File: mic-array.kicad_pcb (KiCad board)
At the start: 2 copper layers, 150 x 150 mm, 70 parts, among them J1 CON40A, K1 74LV244, U1 MIC, U10 MIC, U11 MIC, U12 MIC, U13 MIC, U14 MIC, U15 MIC, U16 MIC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

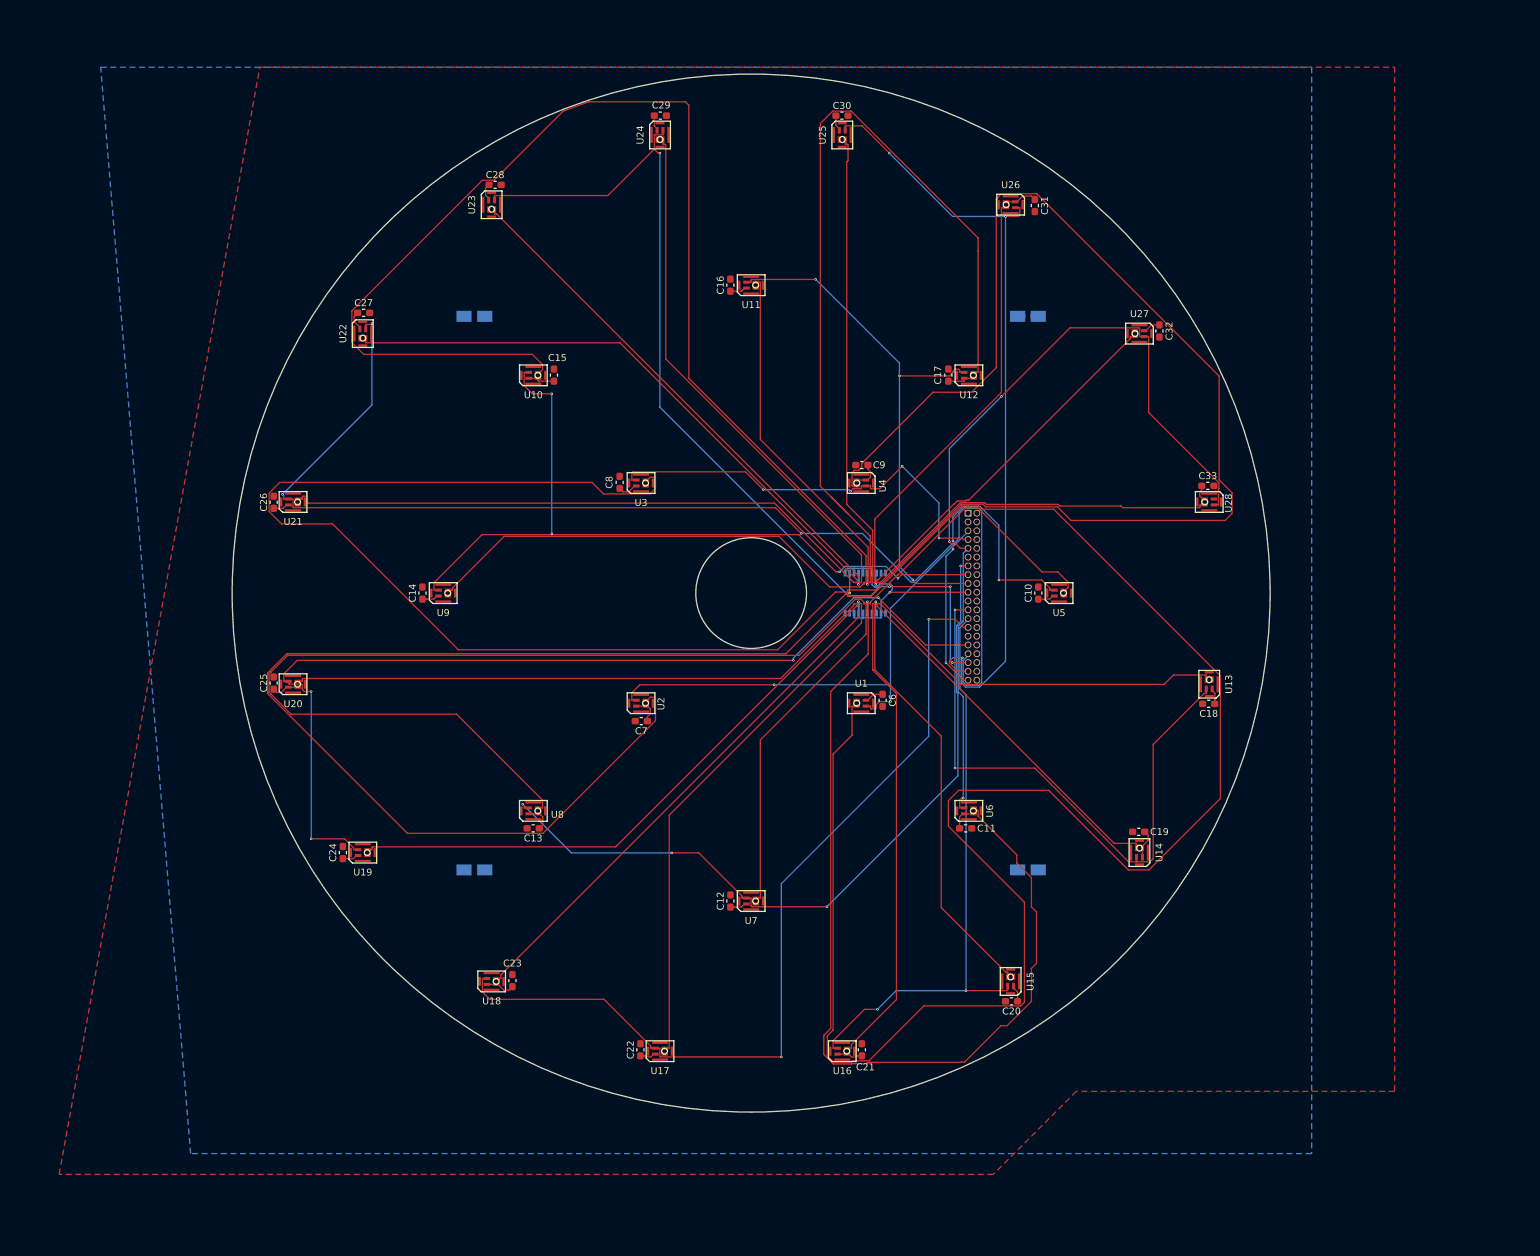
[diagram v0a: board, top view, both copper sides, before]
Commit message: Add new PCB design with improved constraints and routing. Change connector type to 2.54mm one.
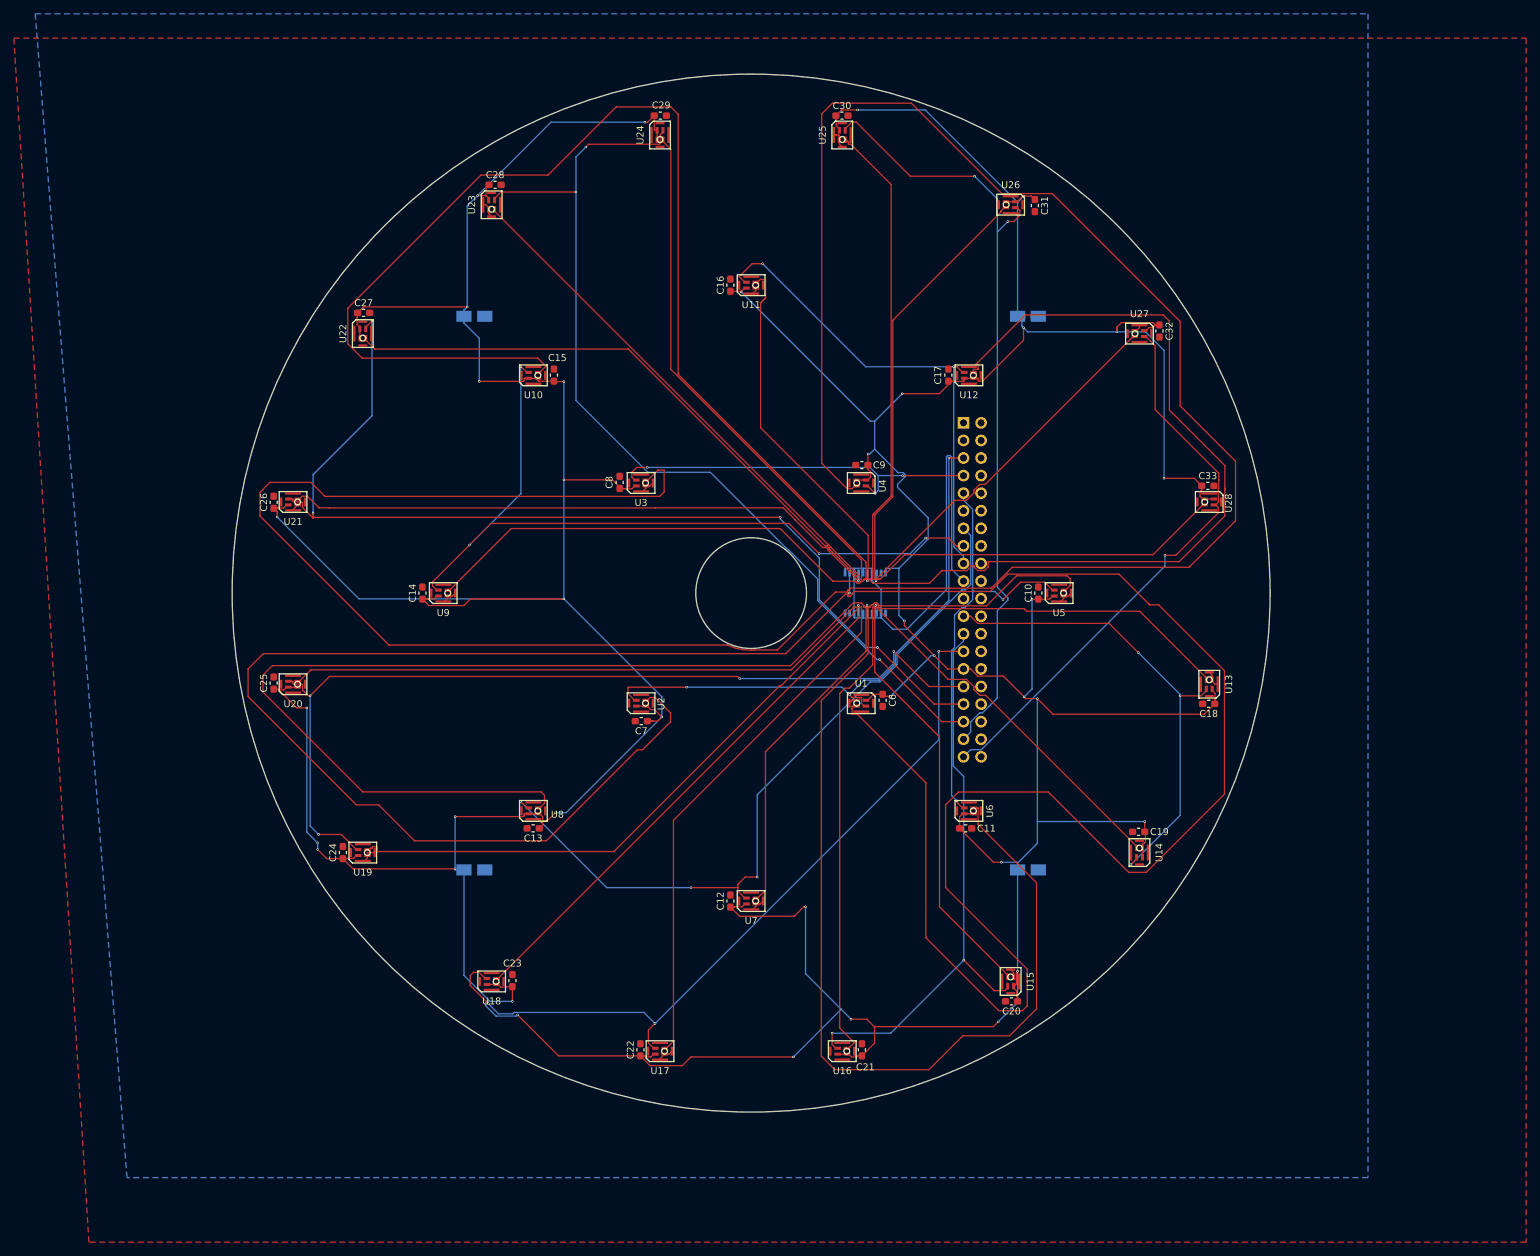
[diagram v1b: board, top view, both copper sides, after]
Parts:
- J1: footprint Connector_PinSocket_1.27mm:PinSocket_2x20_P1.27mm_Vertical -> Connector_PinSocket_2.54mm:PinSocket_2x20_P2.54mm_Vertical
- moved J1 13.1 mm to (180.7, 75.4)
- moved RN2 0.50 mm to (165.5, 102.0)
- moved RN3 0.50 mm to (166.8, 102.0)
- moved RN4 0.50 mm to (165.5, 98.0)
- moved RN5 0.50 mm to (166.8, 98.0)
- moved RN6 0.50 mm to (168.0, 98.0)
- moved RN7 0.50 mm to (168.0, 102.0)
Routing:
- net +3V3: track 87.9 -> 900.7 mm, vias 0 -> 38
- net /CLKIN: track 34.0 -> 77.8 mm, vias 1 -> 0
- net /CLK0_3: track 180.5 -> 215.1 mm
- net /CLK0_0: track 254.9 -> 222.7 mm
- net /DATA10: track 177.8 -> 148.2 mm, vias 3 -> 4
- net GND: track 0.00 -> 28.7 mm
- net /DATA13: track 102.3 -> 83.1 mm, vias 4 -> 1
- net /DATA6: track 87.8 -> 69.3 mm, vias 2 -> 3
- net /DATA8: track 128.8 -> 112.4 mm, vias 2 -> 3
- net /CLK0_1: track 167.8 -> 177.8 mm
- net /DATA9: track 141.7 -> 132.2 mm
- net /DATA0: track 73.6 -> 82.0 mm, vias 2 -> 3
- net /DATA2: track 70.6 -> 62.5 mm, vias 3 -> 2
- net /DATA5: track 78.0 -> 70.2 mm, vias 3 -> 2
- net /CLK0_2: track 158.6 -> 166.1 mm
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
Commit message: Add a new buffer to compensate nets impedance.
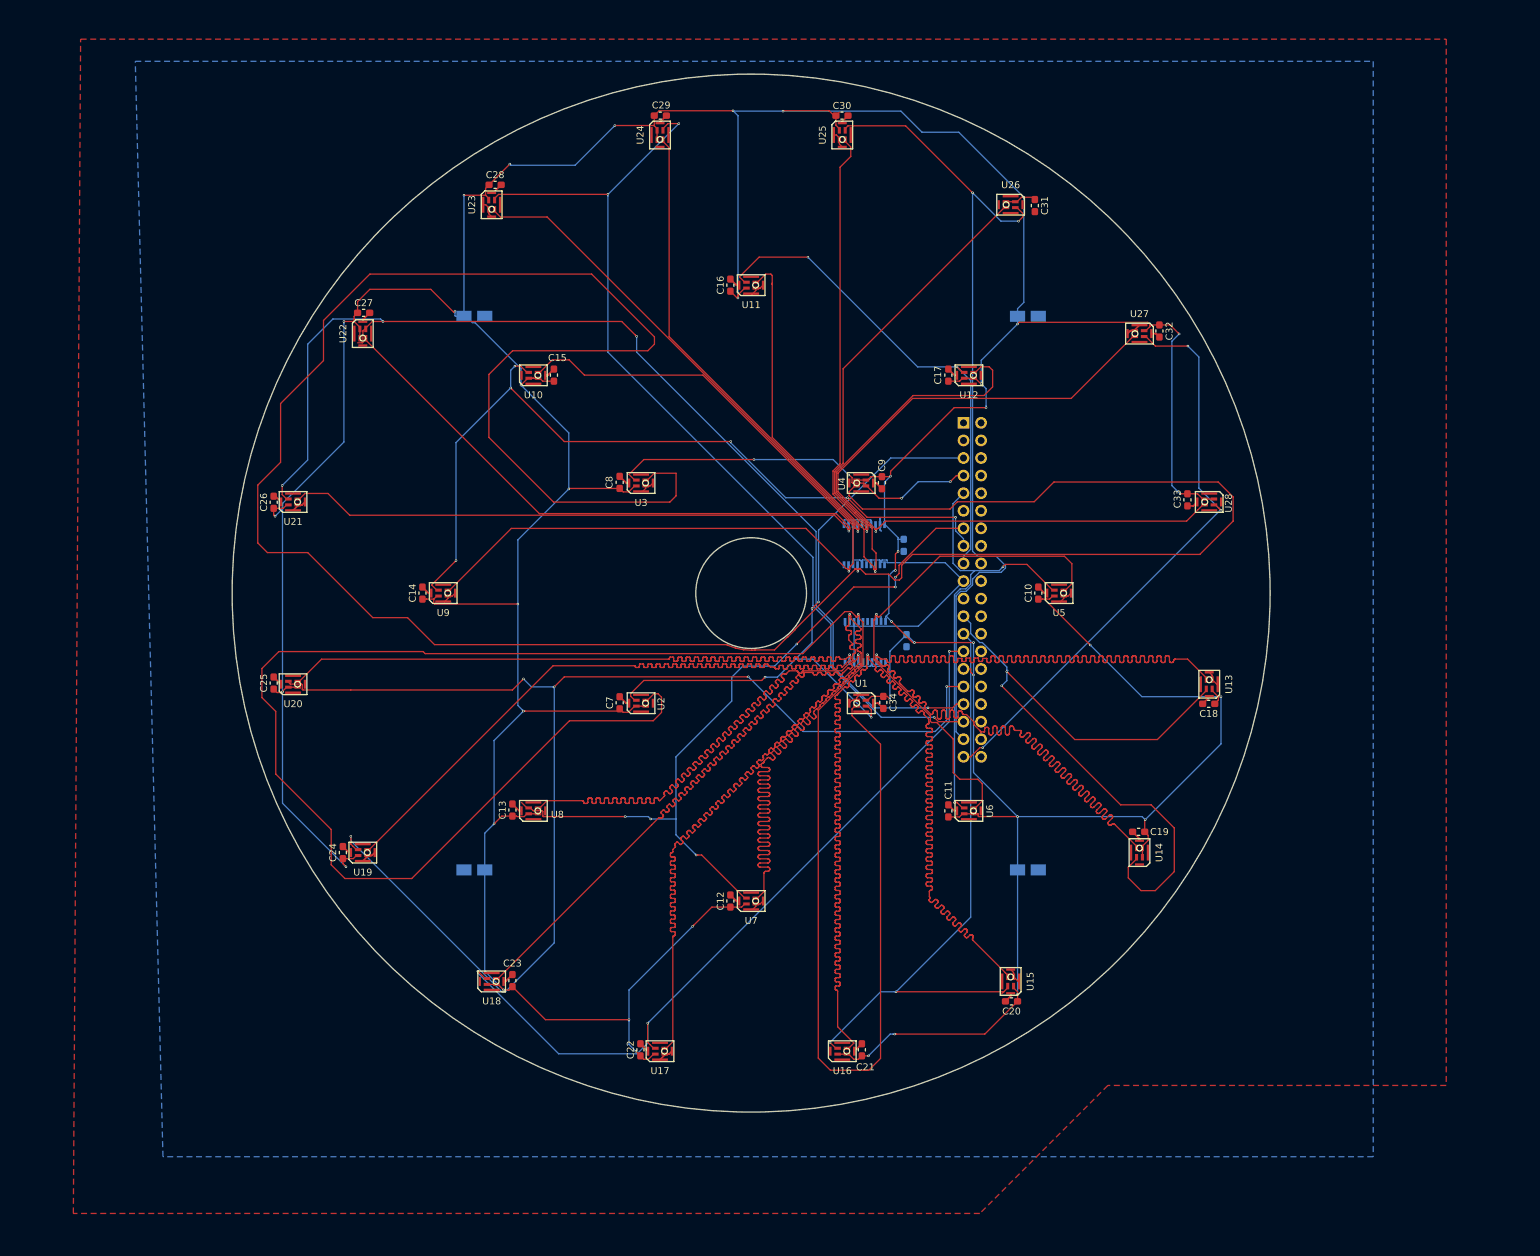
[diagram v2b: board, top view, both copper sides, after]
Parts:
- removed RN1, RN2, RN3, RN4, RN5, RN6, RN7: 0, bridges:bridge_1x4_0.1mm
- added C34: 0.1u, Capacitor_SMD:C_0603_1608Metric_Pad1.05x0.95mm_HandSolder, F.Cu at (169.1, 115.8)
- added K2: 74LV244, Package_SO:SSOP-20_4.4x6.5mm_P0.65mm, B.Cu at (166.3, 93.0)
- added NT1: Tie, bridges:bridge_1x2_0.12mm, F.Cu at (165.5, 103.3)
- added NT10: Tie, bridges:bridge_1x2_0.12mm, F.Cu at (164.2, 109.2)
- added NT11: Tie, bridges:bridge_1x2_0.12mm, F.Cu at (164.1, 90.8)
- added NT12: Tie, bridges:bridge_1x2_0.12mm, F.Cu at (165.4, 90.8)
- added NT13: Tie, bridges:bridge_1x2_0.12mm, F.Cu at (166.7, 90.8)
- added NT14: Tie, bridges:bridge_1x2_0.12mm, F.Cu at (168.0, 90.8)
- added NT2: Tie, bridges:bridge_1x2_0.12mm, F.Cu at (165.4, 96.6)
- added NT3: Tie, bridges:bridge_1x2_0.12mm, F.Cu at (168.1, 103.3)
- added NT4: Tie, bridges:bridge_1x2_0.12mm, F.Cu at (164.2, 103.3)
- added NT5: Tie, bridges:bridge_1x2_0.12mm, F.Cu at (164.1, 96.6)
- added NT6: Tie, bridges:bridge_1x2_0.12mm, F.Cu at (167.9, 96.6)
- added NT7: Tie, bridges:bridge_1x2_0.12mm, F.Cu at (168.2, 109.2)
- added NT8: Tie, bridges:bridge_1x2_0.12mm, F.Cu at (166.8, 109.2)
- added NT9: Tie, bridges:bridge_1x2_0.12mm, F.Cu at (165.5, 109.2)
- C1, C2: value 100u -> 100n; footprint Capacitor_SMD:CP_Elec_3x5.3 -> Capacitor_SMD:C_0603_1608Metric_Pad1.05x0.95mm_HandSolder
- C5: value 100n -> 100u; footprint Capacitor_SMD:C_0603_1608Metric_Pad1.05x0.95mm_HandSolder -> Capacitor_SMD:CP_Elec_3x5.3
- C6: value 0.1u -> 100u; footprint Capacitor_SMD:C_0603_1608Metric_Pad1.05x0.95mm_HandSolder -> Capacitor_SMD:CP_Elec_3x5.3; moved to B.Cu
- moved C2 70.7 mm to (172.4, 106.9), turned to 270 degrees
- moved C6 63.9 mm to (110.0, 140.0), turned to 180 degrees
- moved C1 37.7 mm to (172.1, 93.1), turned to 270 degrees
- moved K1 7.00 mm to (166.5, 107.0)
- moved C7 4.10 mm to (131.0, 115.8), turned to 90 degrees
- moved C13 4.00 mm to (115.5, 131.3), turned to 90 degrees
- moved C9 3.86 mm to (168.9, 84.0), turned to 270 degrees
- moved C33 3.58 mm to (213.1, 86.5), turned to 270 degrees
- moved C11 3.55 mm to (178.5, 131.5), turned to 90 degrees
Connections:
- K1 pad 12: /CLK0 -> /CLK3
- K1 pad 14: /CLK5 -> /CLK0
- K1 pad 16: /CLK2 -> Net-(K1-Pad16)
- K1 pad 18: /CLK6 -> /CLK2
- K1 pad 3: /CLK3 -> /CLK6
- K1 pad 5: /CLK1 -> /CLK7
- K1 pad 7: /CLK4 -> /CLK8
- K1 pad 9: Net-(K1-Pad9) -> /CLK9
- U10 pad 3: /CLK2_1 -> /CLK4_1
- U11 pad 3: /CLK2_2 -> /CLK5_0
- U12 pad 3: /CLK2_3 -> /CLK5_1
- U13 pad 3: /CLK3_0 -> /CLK6_0
- U14 pad 3: /CLK3_1 -> /CLK6_1
- U15 pad 3: /CLK3_2 -> /CLK7_0
- U16 pad 3: /CLK3_3 -> /CLK7_1
- U17 pad 3: /CLK4_0 -> /CLK8_0
- U18 pad 3: /CLK4_1 -> /CLK8_1
- U19 pad 3: /CLK4_2 -> /CLK9_0
- U20 pad 3: /CLK4_3 -> /CLK9_1
- U21 pad 3: /CLK5_0 -> /CLK10_0
- U22 pad 3: /CLK5_1 -> /CLK10_1
- U23 pad 3: /CLK5_2 -> /CLK11_0
- U24 pad 3: /CLK5_3 -> /CLK11_1
- U25 pad 3: /CLK6_0 -> /CLK12_0
- U26 pad 3: /CLK6_1 -> /CLK12_1
- U27 pad 3: /CLK6_2 -> /CLK13_0
- U28 pad 3: /CLK6_3 -> /CLK13_1
- U3 pad 3: /CLK0_2 -> /CLK1_0
- U4 pad 3: /CLK0_3 -> /CLK1_1
- U5 pad 3: /CLK1_0 -> /CLK2_0
- U6 pad 3: /CLK1_1 -> /CLK2_1
- U7 pad 3: /CLK1_2 -> /CLK3_0
- U8 pad 3: /CLK1_3 -> /CLK3_1
- U9 pad 3: /CLK2_0 -> /CLK4_0
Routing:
- net /CLK1_0: track 33.9 -> 263.4 mm
- net /CLK0_3: track 215.1 -> 0.00 mm
- net /CLK0_2: track 166.1 -> 0.00 mm
- net /CLK1_3: track 143.3 -> 0.00 mm
- net /CLK2_1: track 175.1 -> 36.8 mm
- net /CLK2_3: track 122.0 -> 0.00 mm
- net /CLK8_0: track 0.00 -> 100.1 mm
- net /CLK8_1: track 0.00 -> 100.1 mm
- net /CLK9_0: track 0.00 -> 100.0 mm
- net /CLK9_1: track 0.00 -> 100.0 mm
- net /CLK7_0: track 0.00 -> 100.0 mm
- net /CLK7_1: track 0.00 -> 100.0 mm
- net /CLK0_0: track 222.7 -> 130.1 mm
- net /CLK4_2: track 86.4 -> 0.00 mm
- net /CLK4_3: track 85.0 -> 0.00 mm
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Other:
- net class Ground added: clearance 0.12, trace_width 0.25, via_dia 0.35, via_drill 0.2
